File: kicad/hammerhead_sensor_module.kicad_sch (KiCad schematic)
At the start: 8 parts, among them J1 COMMS CONN, J10 Conn_01x06, J4 USB_C_Receptacle_USB2.0_16P

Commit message: finish first pcb revision
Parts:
- removed J10: Conn_01x06, symbol Connector_Generic:Conn_01x06
- removed J4: USB_C_Receptacle_USB2.0_16P, symbol Connector:USB_C_Receptacle_USB2.0_16P
- added D11: SMBJ18A, SMBJ18A:DIOM5436X261N, symbol SMBJ18A:SMBJ18A
- added D19, D20, D4, D6: TPD1E05U06DPYR, TPD1E05U06DPYR:SON65P60X100X45-2N, symbol TPD1E05U06DPYR:TPD1E05U06DPYR
- added J10: 12402012E212A, 12402012E212A:AMPHENOL_12402012E212A, symbol 12402012E212A:12402012E212A
- added J9: B6B-XH-A, B6B-XH-A:B6BXHA, symbol B6B-XH-A:B6B-XH-A
- added U16, U4: TPD4E05U06DQAR, TPD4E05U06DQAR:DQA0010A, symbol TPD4E05U06DQAR:TPD4E05U06DQAR
- C28, C29: footprint (none) -> Capacitor_SMD:C_0201_0603Metric
- R20: footprint Resistor_SMD:R_0402_1005Metric -> Resistor_SMD:R_0201_0603Metric
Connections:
- net 14.8V: now also D11.1, J9.1
- net CC1: now also U16.6 (NC)
- net CC2: now also U16.10 (NC)
- net GND: now also D11.2, D19.2, D20.2, D4.2, D6.2, J10.A1_B12 (GND), J10.B1_A12 (GND), J10.SH1 (SHIELD), J10.SH2 (SHIELD), J10.SH3 (SHIELD), J10.SH4 (SHIELD), J9.2, U16.3 (GND), U16.8 (GND), U4.3 (GND), U4.8 (GND)
- net IR_LED_DIM: now also U4.10 (NC)
- net LASER1: now also U4.6 (NC)
- net LASER2: now also U4.7 (NC)
- net PLATFORM_I2C_SCL: now also D6.1
- net PLATFORM_I2C_SDA: now also D4.1
- net W_LED_DIM: now also U4.9 (NC)
- net 5V renamed VBUS
- net VBUS: now also D19.1, D20.1, J10.A4_B9 (VBUS), J10.B4_A9 (VBUS)
- new net: J9.3, U4.5 (D2-)
- new net: J9.4, U4.4 (D2+)
- new net: J9.5, U4.2 (D1-)
- new net: J9.6, U4.1 (D1+)
- new net: J10.A5 (CC1_A), U16.1 (D1+)
- new net: J10.A6 (D+_A), J10.B6 (D+_B), U16.2 (D1-)
- new net: J10.A7 (D-_A), J10.B7 (D-_B), U16.4 (D2+)
- new net: J10.B5 (CC1_B), U16.5 (D2-)
- new net CM5_HighSpeed/USB2_N: U16.7 (NC)
- new net CM5_HighSpeed/USB2_P: U16.9 (NC)
- no-connect marks 3 -> 2
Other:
- removed sheet Sensor Cluster
- sheet SIM7600G-H-M2B ports: added I2C_SCL_3V3, I2C_SDA_3V3, UART_CTS_3V3, UART_DTR_3V3, UART_RTS_3V3, UART_RXD_3V3, UART_TXD_3V3; removed I2C_SCL, I2C_SDA, UART_CTS, UART_DTR, UART_RTS, UART_RXD, UART_TXD
- moved on the sheet: C28, C29, J1, R1, R2, R20

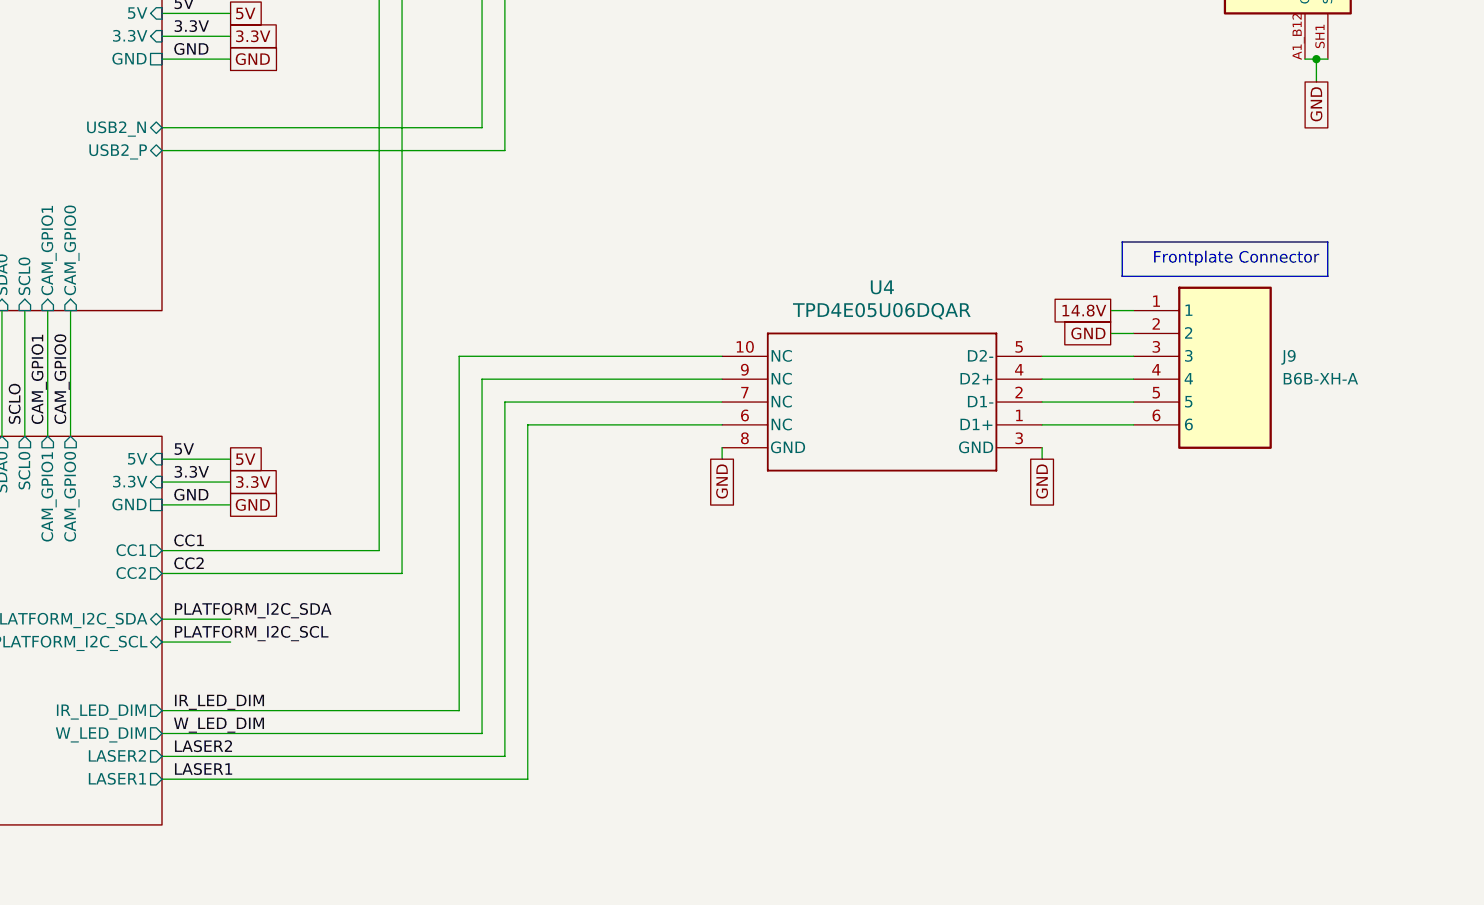
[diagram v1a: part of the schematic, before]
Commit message: add schematic docs and image of robot
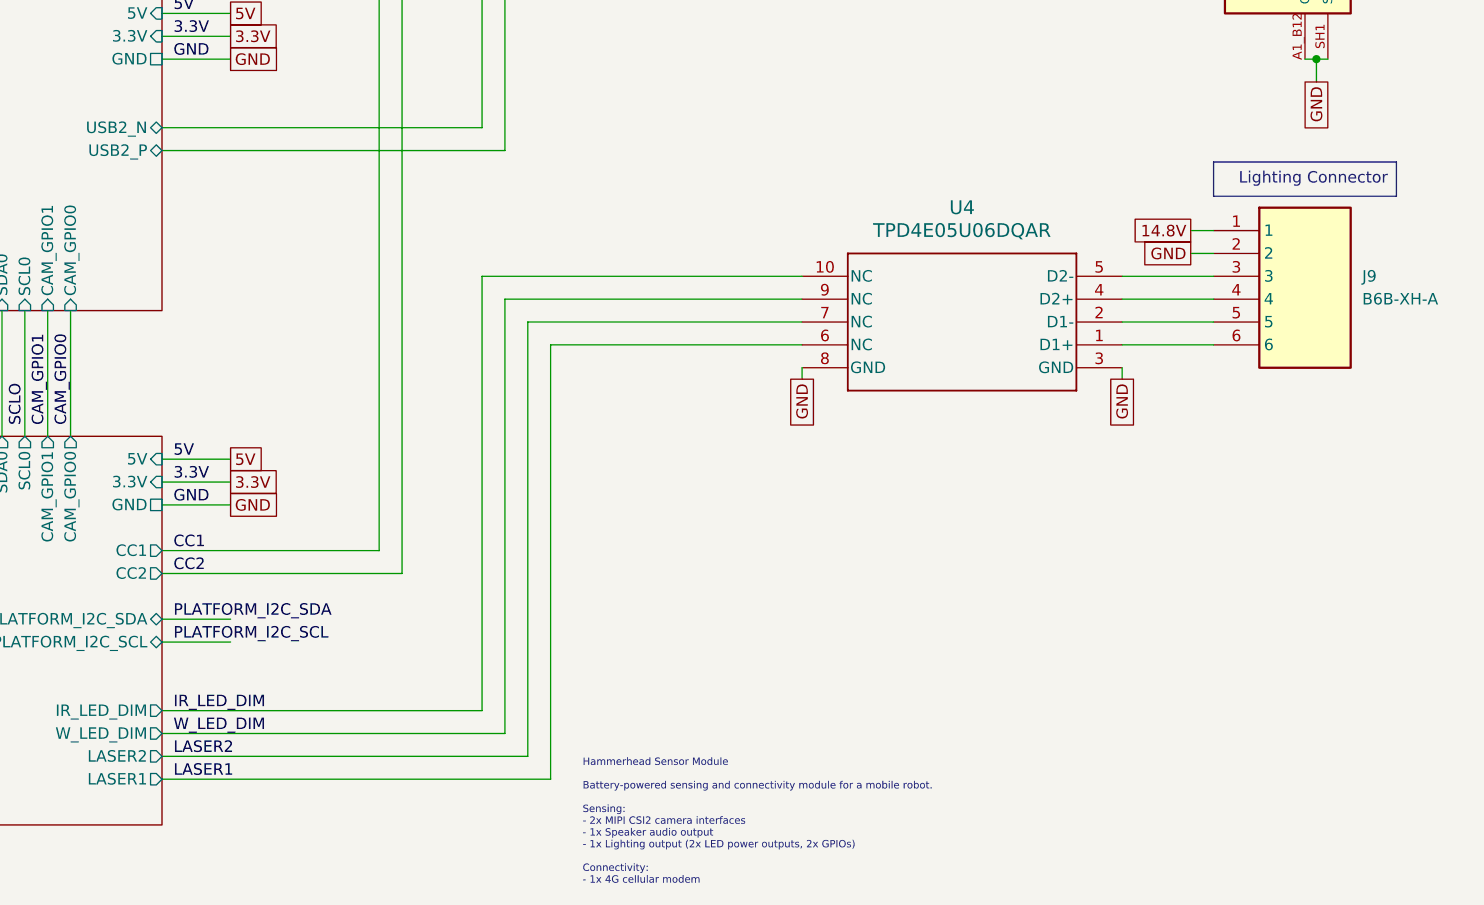
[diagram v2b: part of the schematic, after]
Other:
- note added: "Hammerhead Sensor Module Battery-powered sensing and connectivity module for a mobile robot. Sensing: - 2x MIPI CSI2 camera interfaces - 1x Speaker audio output - 1x Lighting output (2x LED power outputs, 2x GPIOs) Connectivity: - 1x 4G cellular modem"
- moved on the sheet: J9, U4

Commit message: add docs and cleanup
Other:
- note added: "**SMBJ TVS/surge diodes IEC 61000-4-2 level 4 contact discharge: 30kV air-gap discharge: 30kV IEC 61000-4-5 peak pulse power: 600W"
- note added: "**TPDxE05U06 TVS diodes on all connector data signals IEC 61000-4-2 level 4 contact discharge: 12kV air-gap discharge: 15kV IEC 61000-4-5 peak pulse power: 40W"
- moved on the sheet: D11
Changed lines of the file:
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@@
 		)
 	)
+	(text "**SMBJ TVS/surge diodes\n\nIEC 61000-4-2 level 4\n	contact discharge: 30kV\n	air-gap discharge: 30kV\n\nIEC 61000-4-5 peak pulse power: 600W"
+		(exclude_from_sim no)
+		(at 95.758 37.338 0)
+		(effects
+			(font
+				(size 1.016 1.016)
+				(thickness 0.254)
+				(bold yes)
+			)
+		)
+	)
+	(text "**TPDxE05U06 TVS diodes on all connector data signals\n\nIEC 61000-4-2 level 4\n	contact discharge: 12kV\n	air-gap discharge: 15kV\n\nIEC 61000-4-5 peak pulse power: 40W"
+		(exclude_from_sim no)
+		(at 31.242 62.23 0)
+		(effects
+			(font
+				(size 1.016 1.016)
+				(thickness 0.254)
+				(bold yes)
+			)
+			(justify left)
+		)
+	)
 	(text "Discharge Resistor\nNeeded by some\nType C PSUs"
 		(exclude_from_sim no)
@@
 	)
 	(junction
-		(at 116.84 30.48)
+		(at 146.05 30.48)
 		(diameter 0)
 		(color 0 0 0 0)
@@
 	)
 	(junction
-		(at 88.9 30.48)
+		(at 118.11 30.48)
 		(diameter 0)
 		(color 0 0 0 0)
@@
 	)
 	(junction
-		(at 74.93 27.94)
+		(at 243.84 66.04)
 		(diameter 0)
 		(color 0 0 0 0)
 	)
 	(junction
-		(at 243.84 66.04)
+		(at 118.11 27.94)
 		(diameter 0)
 		(color 0 0 0 0)
 	)
 	(junction
-		(at 88.9 27.94)
+		(at 38.1 33.02)
 		(diameter 0)
 		(color 0 0 0 0)
 	)
 	(junction
-		(at 38.1 33.02)
+		(at 73.66 27.94)
 		(diameter 0)
 		(color 0 0 0 0)
@@
 	(wire
 		(pts
-			(xy 116.84 30.48) (xy 116.84 45.72)
+			(xy 146.05 30.48) (xy 146.05 45.72)
 		)
 		(stroke
@@
 	(wire
 		(pts
-			(xy 113.03 27.94) (xy 121.92 27.94)
+			(xy 142.24 27.94) (xy 151.13 27.94)
 		)
 		(stroke
@@
 	(wire
 		(pts
-			(xy 74.93 27.94) (xy 88.9 27.94)
-		)
-		(stroke
-			(width 0)
-			(type default)
-		)
-	)
-	(wire
-		(pts
 			(xy 154.94 58.42) (xy 154.94 143.51)
 		)
@@
 	(wire
 		(pts
-			(xy 116.84 30.48) (xy 121.92 30.48)
+			(xy 146.05 30.48) (xy 151.13 30.48)
 		)
 		(stroke
@@
 	(wire
 		(pts
-			(xy 113.03 30.48) (xy 116.84 30.48)
+			(xy 142.24 30.48) (xy 146.05 30.48)
 		)
 		(stroke
@@
 	(wire
 		(pts
-			(xy 88.9 27.94) (xy 92.71 27.94)
+			(xy 118.11 27.94) (xy 121.92 27.94)
 		)
 		(stroke
@@
 	(wire
 		(pts
-			(xy 88.9 26.67) (xy 88.9 27.94)
+			(xy 118.11 26.67) (xy 118.11 27.94)
 		)
 		(stroke
@@
 	(wire
 		(pts
-			(xy 113.03 25.4) (xy 121.92 25.4)
+			(xy 142.24 25.4) (xy 151.13 25.4)
 		)
 		(stroke
@@
 	(wire
 		(pts
+			(xy 73.66 27.94) (xy 118.11 27.94)
+		)
+		(stroke
+			(width 0)
+			(type default)
+		)
+	)
+	(wire
+		(pts
 			(xy 166.37 96.52) (xy 166.37 60.96)
 		)
@@
 	(wire
 		(pts
-			(xy 31.75 27.94) (xy 74.93 27.94)
+			(xy 31.75 27.94) (xy 73.66 27.94)
 		)
 		(stroke
@@
 	(wire
 		(pts
-			(xy 88.9 30.48) (xy 92.71 30.48)
+			(xy 118.11 30.48) (xy 121.92 30.48)
 		)
 		(stroke
@@
 	(wire
 		(pts
-			(xy 31.75 30.48) (xy 88.9 30.48)
+			(xy 31.75 30.48) (xy 118.11 30.48)
 		)
 		(stroke
@@
 	(wire
 		(pts
-			(xy 88.9 31.75) (xy 88.9 30.48)
+			(xy 118.11 31.75) (xy 118.11 30.48)
 		)
 		(stroke
@@
 	(wire
 		(pts
-			(xy 67.31 45.72) (xy 116.84 45.72)
+			(xy 67.31 45.72) (xy 146.05 45.72)
 		)
 		(stroke
@@
 	)
 	(label "3.3V"
-		(at 114.3 30.48 0)
+		(at 143.51 30.48 0)
 		(effects
 			(font
@@
 	)
 	(label "5V"
-		(at 114.3 25.4 0)
+		(at 143.51 25.4 0)
 		(effects
 			(font
@@
 	)
 	(label "4V"
-		(at 114.3 27.94 0)
+		(at 143.51 27.94 0)
 		(effects
 			(font
@@
 	(global_label "GND"
 		(shape passive)
-		(at 74.93 38.1 270)
+		(at 73.66 38.1 270)
 		(fields_autoplaced yes)
 		(effects
@@
 		)
 		(property "Intersheetrefs" "${INTERSHEET_REFS}"
-			(at 74.93 43.8444 90)
+			(at 73.66 43.8444 90)
 			(effects
 				(font
@@
 	(global_label "3.3V"
 		(shape passive)
-		(at 121.92 30.48 0)
+		(at 151.13 30.48 0)
 		(fields_autoplaced yes)
 		(effects
@@
 		)
 		(property "Intersheetrefs" "${INTERSHEET_REFS}"
-			(at 127.9063 30.48 0)
+			(at 157.1163 30.48 0)
 			(effects
 				(font
@@
 	(global_label "GND"
 		(shape passive)
-		(at 88.9 31.75 270)
+		(at 118.11 31.75 270)
 		(fields_autoplaced yes)
 		(effects
@@
 		)
 		(property "Intersheetrefs" "${INTERSHEET_REFS}"
-			(at 88.9 37.4944 90)
+			(at 118.11 37.4944 90)
 			(effects
 				(font
@@
 	(global_label "4V"
 		(shape passive)
-		(at 121.92 27.94 0)
+		(at 151.13 27.94 0)
 		(fields_autoplaced yes)
 		(effects
@@
 		)
 		(property "Intersheetrefs" "${INTERSHEET_REFS}"
-			(at 126.092 27.94 0)
+			(at 155.302 27.94 0)
 			(effects
 				(font
@@
 	(global_label "5V"
 		(shape passive)
-		(at 121.92 25.4 0)
+		(at 151.13 25.4 0)
 		(fields_autoplaced yes)
 		(effects
@@
 		)
 		(property "Intersheetrefs" "${INTERSHEET_REFS}"
-			(at 126.092 25.4 0)
+			(at 155.302 25.4 0)
 			(effects
 				(font
@@
 	(global_label "14.8V"
 		(shape passive)
-		(at 88.9 26.67 90)
+		(at 118.11 26.67 90)
 		(fields_autoplaced yes)
 		(effects
@@
 		)
 		(property "Intersheetrefs" "${INTERSHEET_REFS}"
-			(at 88.9 19.4742 90)
+			(at 118.11 19.4742 90)
 			(effects
 				(font
@@
 	(symbol
 		(lib_id "SMBJ18A:SMBJ18A")
-		(at 74.93 33.02 90)
+		(at 73.66 33.02 90)
 		(unit 1)
 		(exclude_from_sim no)
@@
 		(fields_autoplaced yes)
 		(property "Reference" "D11"
-			(at 77.47 31.7499 90)
+			(at 76.2 31.7499 90)
 			(effects
 				(font
@@
 		)
 		(property "Value" "SMBJ18A"
-			(at 77.47 34.2899 90)
+			(at 76.2 34.2899 90)
 			(effects
 				(font
@@
 		)
 		(property "Footprint" "SMBJ18A:DIOM5436X261N"
-			(at 74.93 33.02 0)
+			(at 73.66 33.02 0)
 			(effects
 				(font
@@
 		)
 		(property "Datasheet" ""
-			(at 74.93 33.02 0)
+			(at 73.66 33.02 0)
 			(effects
 				(font
@@
 		)
 		(property "Description" ""
-			(at 74.93 33.02 0)
+			(at 73.66 33.02 0)
 			(effects
 				(font
@@
 		)
 		(property "MF" "Littelfuse Inc."
-			(at 74.93 33.02 0)
+			(at 73.66 33.02 0)
 			(effects
 				(font
@@
 		)
 		(property "MAXIMUM_PACKAGE_HEIGHT" "2.61"
-			(at 74.93 33.02 0)
+			(at 73.66 33.02 0)
 			(effects
 				(font
@@
 		)
 		(property "CREATOR" "ASHISH"
-			(at 74.93 33.02 0)
+			(at 73.66 33.02 0)
 			(effects
 				(font
@@
 		)
 		(property "Price" "None"
-			(at 74.93 33.02 0)
+			(at 73.66 33.02 0)
 			(effects
 				(font
@@
 		)
 		(property "Package" "None"
-			(at 74.93 33.02 0)
+			(at 73.66 33.02 0)
 			(effects
 				(font
@@
 		)
 		(property "Check_prices" "https://www.snapeda.com/parts/SMBJ18A/Littelfuse/view-part/?ref=eda"
-			(at 74.93 33.02 0)
+			(at 73.66 33.02 0)
 			(effects
 				(font
@@
 		)
 		(property "STANDARD" "IPC-7351B"
-			(at 74.93 33.02 0)
+			(at 73.66 33.02 0)
 			(effects
 				(font
@@
 		)
 		(property "PARTREV" "JC.07/04/25 v4"
-			(at 74.93 33.02 0)
+			(at 73.66 33.02 0)
 			(effects
 				(font
@@
 		)
 		(property "VERIFIER" ""
-			(at 74.93 33.02 0)
+			(at 73.66 33.02 0)
 			(effects
 				(font
@@
 		)
 		(property "SnapEDA_Link" "https://www.snapeda.com/parts/SMBJ18A/Littelfuse/view-part/?ref=snap"
-			(at 74.93 33.02 0)
+			(at 73.66 33.02 0)
 			(effects
 				(font
@@
 		)
 		(property "MP" "SMBJ18A"
-			(at 74.93 33.02 0)
+			(at 73.66 33.02 0)
 			(effects
 				(font
@@
 		)
 		(property "Description_1" "TVS Diode, 600W, 18V, -65 to 150 Operating Temp, Surface Mount, SMBJ Series | Littelfuse SMBJ18A"
-			(at 74.93 33.02 0)
+			(at 73.66 33.02 0)
 			(effects
 				(font
@@
 		)
 		(property "Availability" "In Stock"
-			(at 74.93 33.02 0)
+			(at 73.66 33.02 0)
 			(effects
 				(font
@@
 		)
 		(property "MANUFACTURER" "Littelfuse"
-			(at 74.93 33.02 0)
+			(at 73.66 33.02 0)
 			(effects
 				(font
@@
 	)
 	(sheet
-		(at 92.71 22.86)
+		(at 121.92 22.86)
 		(size 20.32 10.16)
 		(exclude_from_sim no)
@@
 		)
 		(property "Sheetname" "Power"
-			(at 92.71 22.1484 0)
+			(at 121.92 22.1484 0)
 			(effects
 				(font
@@
 		)
 		(property "Sheetfile" "power.kicad_sch"
-			(at 92.71 33.6046 0)
+			(at 121.92 33.6046 0)
 			(effects
 				(font
@@
 		)
 		(pin "5V" output
-			(at 113.03 25.4 0)
+			(at 142.24 25.4 0)
 			(effects
 				(font
@@
 		)
 		(pin "GND" passive
-			(at 92.71 30.48 180)
+			(at 121.92 30.48 180)
 			(effects
 				(font
@@
 		)
 		(pin "4V" output
-			(at 113.03 27.94 0)
+			(at 142.24 27.94 0)
 			(effects
 				(font
@@
 		)
 		(pin "14.8V" input
-			(at 92.71 27.94 180)
+			(at 121.92 27.94 180)
 			(effects
 				(font
@@
 		)
 		(pin "3.3V" output
-			(at 113.03 30.48 0)
+			(at 142.24 30.48 0)
 			(effects
 				(font

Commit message: add power testpoints, add debug gpio testpoints, add comms testpoints, add logo, add component orientation silkscreen, add board name and revision silkscreen
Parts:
- added TP10, TP11, TP12, TP13, TP14, TP15, TP16, TP5, TP6, TP7, TP8, TP9: TestPoint, TestPoint:TestPoint_Pad_1.0x1.0mm, symbol Connector:TestPoint
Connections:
- net 14.8V: now also TP11.1
- net 3.3V: now also TP14.1
- net 4V: now also TP13.1
- net PLATFORM_I2C_SCL: now also TP8.1
- net PLATFORM_I2C_SDA: now also TP7.1
- net SIM_I2C_SCL: now also TP6.1
- net SIM_I2C_SDA: now also TP5.1
- net SIM_UART_RXD: now also TP16.1
- net SIM_UART_TXD: now also TP15.1
- net USB3-0-D_N: now also TP9.1
- net USB3-0-D_P: now also TP10.1
- net VBUS: now also TP12.1
- net CM5_HighSpeed/USB2_N renamed USB2_N
- net CM5_HighSpeed/USB2_P renamed USB2_P
